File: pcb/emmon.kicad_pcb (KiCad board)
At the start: 2 copper layers, 114.3 x 97.8 mm, 37 parts, among them J1 PULSES_CONNECTOR, J2 Conn_01x06, J3 POWER_CONNECTOR, U1 DS3231MZ, U2 AT24CS32-SSHM, U3 ESP-12E, U4 Ai-Thinker-Ra-01, U5 AMS1117-3.3

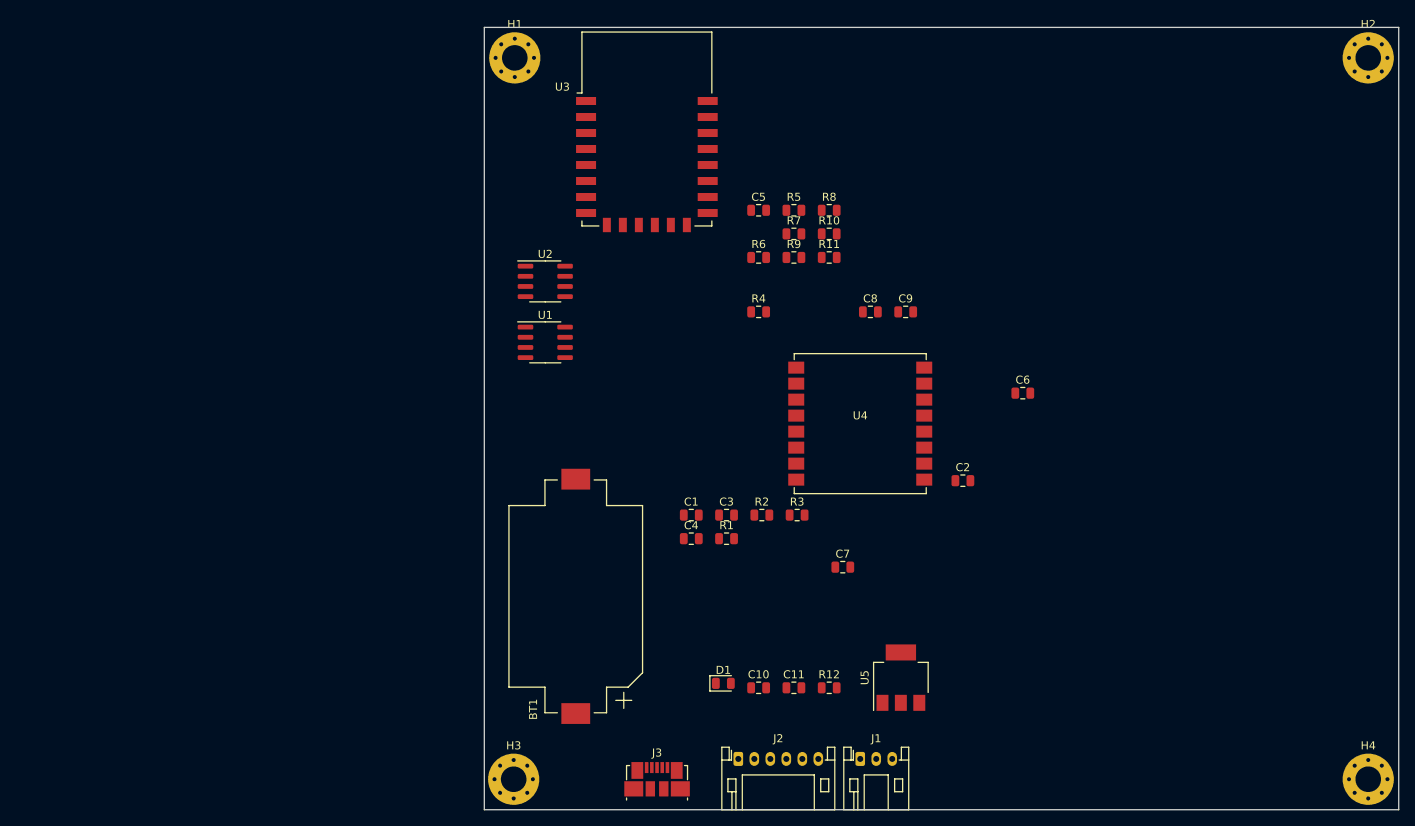
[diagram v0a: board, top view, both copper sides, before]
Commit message: se avanza en el ruteo de pistas
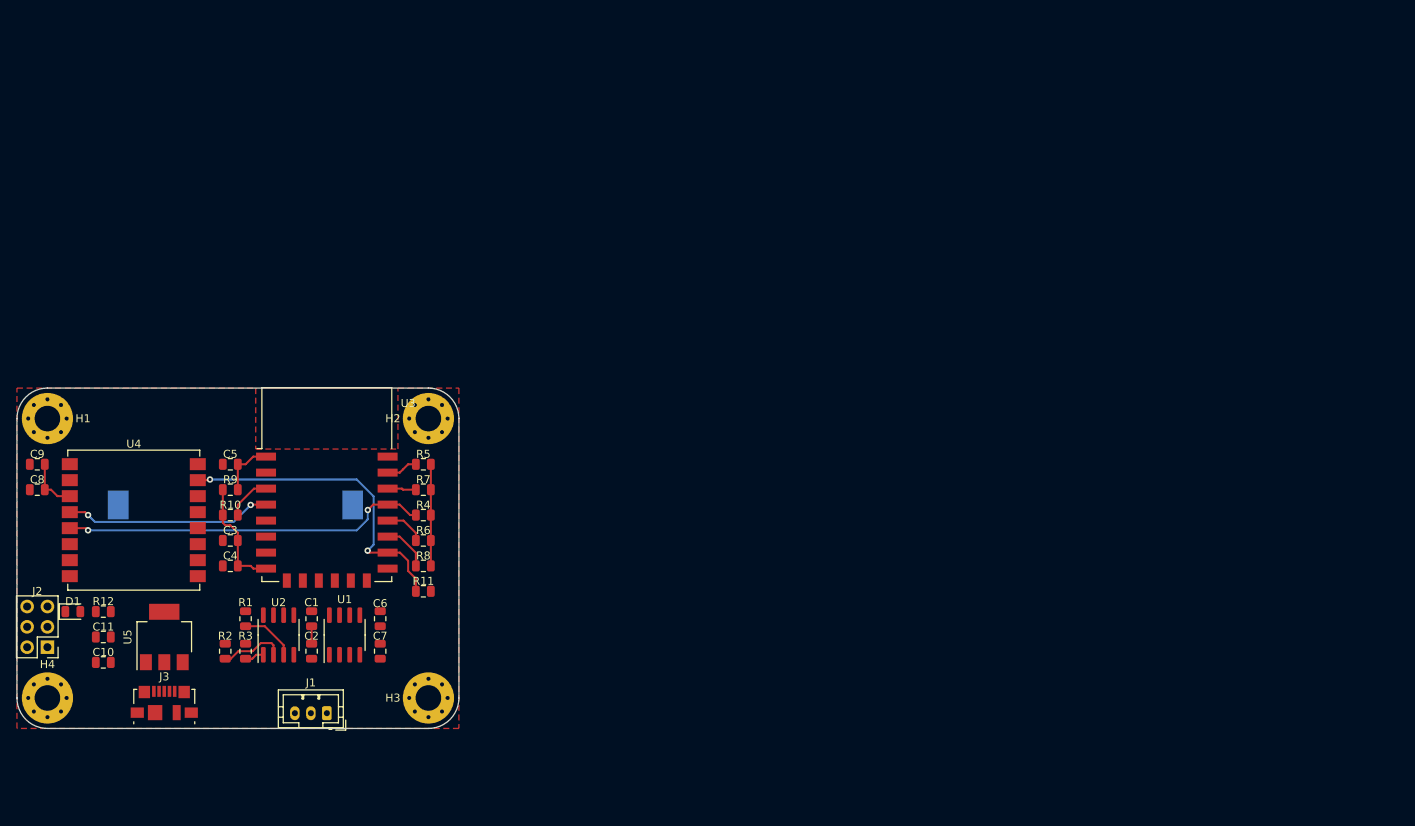
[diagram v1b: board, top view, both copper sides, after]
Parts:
- BT1: moved to B.Cu
- J1: footprint Connector_JST:JST_PH_S3B-PH-K_1x03_P2.00mm_Horizontal -> Connector_JST:JST_PH_B3B-PH-K_1x03_P2.00mm_Vertical
- J2: value Conn_01x06 -> PROG_CONNECTOR; footprint Connector_JST:JST_PH_S6B-PH-K_1x06_P2.00mm_Horizontal -> Connector_PinHeader_2.54mm:PinHeader_2x03_P2.54mm_Vertical
- moved H4 165.4 mm to (99.1, 118.1)
- moved H2 125.8 mm to (146.7, 83.2)
- moved C9 110.2 mm to (97.8, 88.9), turned to 180 degrees
- moved C8 106.5 mm to (97.8, 92.1), turned to 180 degrees
- moved U5 92.2 mm to (113.7, 110.5)
- moved U4 91.6 mm to (109.9, 95.9)
- moved R12 91.2 mm to (106.0, 107.3)
- moved J2 87.5 mm to (99.1, 111.8), turned to 180 degrees
- moved C11 86.6 mm to (106.0, 110.5), turned to 180 degrees
- moved C6 85.1 mm to (140.7, 108.2), turned to 270 degrees
- moved C2 84.2 mm to (132.1, 112.3), turned to 270 degrees
- moved R10 82.7 mm to (121.9, 95.2)
- moved C10 82.0 mm to (106.0, 113.7)
- moved D1 81.8 mm to (102.2, 107.3)
- moved R9 76.2 mm to (121.9, 92.1)
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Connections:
- J2 pad 2: TX -> (no net)
- J2 pad 3: ALARM -> GND
- J2 pad 4: PULSES -> (no net)
- J2 pad 5: RST -> (no net)
- J2 pad 6: GND -> (no net)
- J3 pad 6: Net-(J3-Pad6) -> GND
- U3 pad 22: TX -> (no net)
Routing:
- net DIO0: track 0.00 -> 45.9 mm, vias 0 -> 2
- net NSS: track 0.00 -> 39.8 mm, vias 0 -> 2
- net +3V3: track 0.00 -> 35.9 mm
- net RESET: track 0.00 -> 25.9 mm, vias 0 -> 2
- net Net-(R2-Pad2): track 0.00 -> 8.15 mm
- net RST: track 0.00 -> 7.10 mm
- net Net-(R1-Pad2): track 0.00 -> 6.95 mm
- net SDA: track 0.00 -> 6.00 mm
- net Net-(R10-Pad2): track 0.00 -> 5.65 mm
- net PULSES: track 0.00 -> 5.11 mm
- net ALARM: track 0.00 -> 3.96 mm
- net SCL: track 0.00 -> 3.58 mm
- net Net-(R3-Pad2): track 0.00 -> 2.43 mm
- added copper zone on F.Cu, net GND
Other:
- board size 114.3 x 97.8 mm -> 55.2 x 42.5 mm

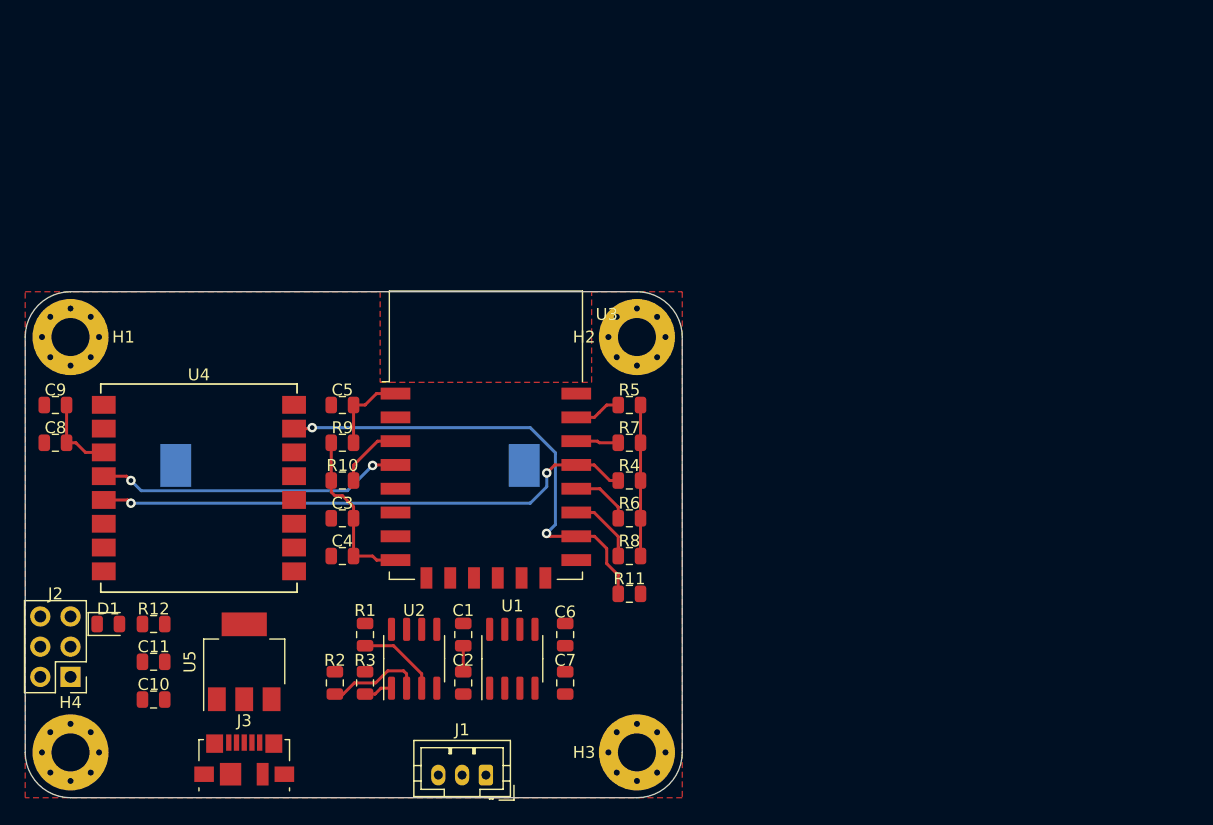
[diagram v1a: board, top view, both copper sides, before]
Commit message: se completa el esquemático y se avanza en el posicionamiento del pcb
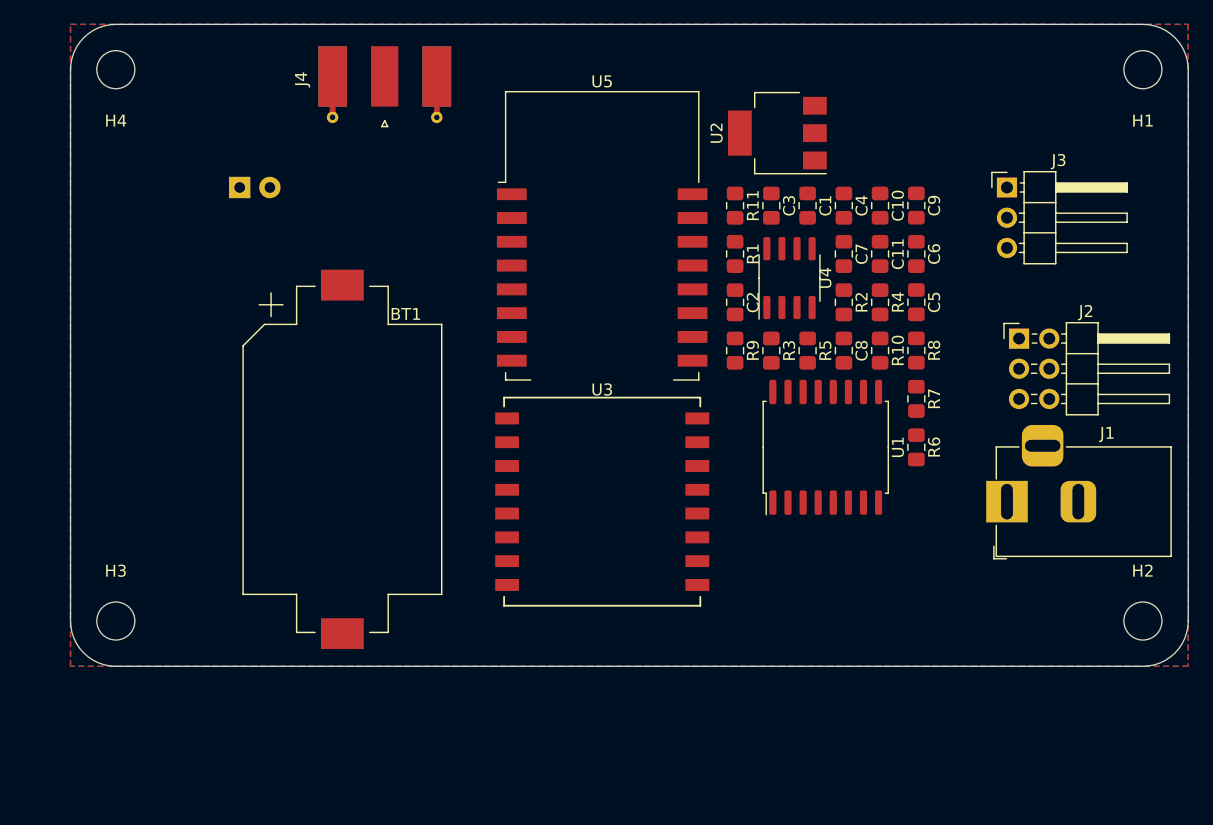
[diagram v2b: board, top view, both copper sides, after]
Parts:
- removed R12: 12K, Resistor_SMD:R_0805_2012Metric
- added J4: ANTENNA_CONNECTOR, Connector_Coaxial:SMA_Molex_73251-1153_EdgeMount_Horizontal, F.Cu at (125.5, 63.0)
- BT1: moved to F.Cu
- C1: footprint Capacitor_SMD:C_0805_2012Metric -> Capacitor_SMD:C_0805_2012Metric_Pad1.15x1.40mm_HandSolder
- C10: value 10u -> 1u; footprint Capacitor_SMD:C_0805_2012Metric -> Capacitor_SMD:C_0805_2012Metric_Pad1.15x1.40mm_HandSolder
- C11, C3, C6, C8: value 10u -> 100n; footprint Capacitor_SMD:C_0805_2012Metric -> Capacitor_SMD:C_0805_2012Metric_Pad1.15x1.40mm_HandSolder
- C2: value 100n -> 1u; footprint Capacitor_SMD:C_0805_2012Metric -> Capacitor_SMD:C_0805_2012Metric_Pad1.15x1.40mm_HandSolder
- C4: value 100n -> 10u; footprint Resistor_SMD:R_0805_2012Metric -> Capacitor_SMD:C_0805_2012Metric_Pad1.15x1.40mm_HandSolder
- C5: value 47p -> 10u; footprint Capacitor_SMD:C_0805_2012Metric -> Capacitor_SMD:C_0805_2012Metric_Pad1.15x1.40mm_HandSolder
- C7: value 100n -> 1u; footprint Resistor_SMD:R_0805_2012Metric -> Capacitor_SMD:C_0805_2012Metric_Pad1.15x1.40mm_HandSolder
- C9: value 100n -> 470p; footprint Resistor_SMD:R_0805_2012Metric -> Capacitor_SMD:C_0805_2012Metric_Pad1.15x1.40mm_HandSolder
- D1: footprint LED_SMD:LED_0805_2012Metric -> LED_THT:LED_D3.0mm; moved to B.Cu
- H1, H2, H3, H4: value MountingHole_Pad -> MountingHole; footprint MountingHole:MountingHole_3.2mm_M3_Pad_Via -> MountingHole:MountingHole_3.2mm_M3
- J1: value PULSES_CONNECTOR -> POWER_CONNECTOR; footprint Connector_JST:JST_PH_B3B-PH-K_1x03_P2.00mm_Vertical -> Connector_BarrelJack:BarrelJack_Horizontal
- J2: footprint Connector_PinHeader_2.54mm:PinHeader_2x03_P2.54mm_Vertical -> Connector_PinHeader_2.54mm:PinHeader_2x03_P2.54mm_Horizontal
- J3: value POWER_CONNECTOR -> SENSOR_CONNECTOR; footprint Connector_USB:USB_Micro-B_Molex_47346-0001 -> Connector_PinHeader_2.54mm:PinHeader_1x03_P2.54mm_Horizontal
- R1, R10, R11, R2, R3, R4, R5, R6, R7, R8, R9: footprint Resistor_SMD:R_0805_2012Metric -> Resistor_SMD:R_0805_2012Metric_Pad1.15x1.40mm_HandSolder
- U1: value DS3231MZ -> DS3231M; footprint Package_SO:SOIC-8_3.9x4.9mm_P1.27mm -> Package_SO:SOIC-16W_7.5x10.3mm_P1.27mm
- U2: value AT24CS32-SSHM -> AMS1117-3.3; footprint Package_SO:SOIC-8_3.9x4.9mm_P1.27mm -> Package_TO_SOT_SMD:SOT-223-3_TabPin2
- U3: value ESP-12E -> Ai-Thinker-Ra-01; footprint RF_Module:ESP-12E -> RF_Module:Ai-Thinker-Ra-01-LoRa
- U4: value Ai-Thinker-Ra-01 -> AT24CS32-SSHM; footprint RF_Module:Ai-Thinker-Ra-01-LoRa -> Package_SO:SOIC-8_3.9x4.9mm_P1.27mm
- U5: value AMS1117-3.3 -> ESP-12S; footprint Package_TO_SOT_SMD:SOT-223-3_TabPin2 -> ESP8266:ESP-12S
- moved H1 92.9 mm to (189.2, 60.7)
- moved J2 84.7 mm to (178.8, 83.3), turned to 0 degrees
- moved J3 80.2 mm to (177.8, 70.6)
- moved C9 74.3 mm to (170.2, 72.1), turned to 270 degrees
- moved C10 73.9 mm to (167.1, 72.1), turned to 90 degrees
- moved C11 70.1 mm to (167.1, 76.2), turned to 270 degrees
- moved C8 66.7 mm to (164.1, 84.3), turned to 90 degrees
- moved H4 57.5 mm to (102.9, 60.7)
- moved U2 53.7 mm to (158.5, 66.0), turned to 180 degrees
- moved R2 53.4 mm to (164.1, 80.3), turned to 90 degrees
- moved U4 52.7 mm to (159.5, 78.2), turned to 90 degrees
- moved C4 51.4 mm to (164.1, 72.1), turned to 270 degrees
- moved J1 49.5 mm to (177.8, 97.0)
- moved C5 49.0 mm to (170.2, 80.3), turned to 270 degrees
- moved H2 48.8 mm to (189.2, 107.1)
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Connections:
- C1 pad 1: +3V3 -> GND
- C1 pad 2: GND -> +5V
- C10 pad 1: GND -> +3V3
- C10 pad 2: +5V -> GND
- C5 pad 1: RST -> +3V3
- C9 pad 1: +3V3 -> RST
- H1 pad 1: GND -> (no net)
- H2 pad 1: GND -> (no net)
- H3 pad 1: GND -> (no net)
- H4 pad 1: GND -> (no net)
- J1 pad 1: +3V3 -> +5V
- J1 pad 2: PULSES -> GND
- J2 pad 1: +3V3 -> TX
- J2 pad 2: (no net) -> +3V3
- J2 pad 3: GND -> RST
- J2 pad 5: (no net) -> RX
- J2 pad 6: (no net) -> GND
- J3 pad 1: +5V -> +3V3
- J3 pad 2: (no net) -> PULSES
- J3 pad 3: (no net) -> GND
- R1 pad 1: +3V3 -> Net-(D1-Pad2)
- R1 pad 2: Net-(R1-Pad2) -> +3V3
- R10 pad 2: Net-(R10-Pad2) -> RST
- R4 pad 2: DIO0 -> Net-(R4-Pad2)
- R5 pad 1: +3V3 -> SDA
- R5 pad 2: ALARM -> +3V3
- R6 pad 1: +3V3 -> SCL
- R6 pad 2: PULSES -> +3V3
- R7 pad 1: +3V3 -> PULSES
- R7 pad 2: SCL -> +3V3
- R8 pad 1: +3V3 -> ALARM
- R8 pad 2: SDA -> +3V3
- R9 pad 1: +3V3 -> EN
- R9 pad 2: RST -> +3V3
- U1 pad 2: +3V3 -> +BATT
- U1 pad 6: +BATT -> GND
- U1 pad 7: SDA -> GND
- U1 pad 8: SCL -> GND
- U2 pad 1: Net-(R3-Pad2) -> GND
- U2 pad 2: Net-(R2-Pad2) -> +3V3
- U2 pad 3: Net-(R1-Pad2) -> +5V
- U3 pad 1: RST -> ANT
- U3 pad 12: (no net) -> SCK
- U3 pad 13: (no net) -> MISO
- U3 pad 14: (no net) -> MOSI
- U3 pad 15: GND -> NSS
- U3 pad 16: NSS -> GND
- U3 pad 2: (no net) -> GND
- U3 pad 3: Net-(R10-Pad2) -> +3V3
- U3 pad 5: SCK -> (no net)
- U3 pad 6: MISO -> (no net)
- U3 pad 7: MOSI -> (no net)
- U3 pad 8: +3V3 -> (no net)
- U3 pad 9: (no net) -> GND
- U4 pad 1: (no net) -> Net-(R4-Pad2)
- U4 pad 2: GND -> Net-(R3-Pad2)
- U4 pad 3: +3V3 -> Net-(R2-Pad2)
- U4 pad 4: RESET -> GND
- U4 pad 5: DIO0 -> SDA
- U4 pad 6: (no net) -> SCL
- U4 pad 7: (no net) -> GND
- U4 pad 8: (no net) -> +3V3
- U5 pad 1: GND -> RST
- U5 pad 2: +3V3 -> (no net)
- U5 pad 3: +5V -> EN
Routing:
- net DIO0: track 45.9 -> 0.00 mm, vias 2 -> 0
- net NSS: track 39.8 -> 0.00 mm, vias 2 -> 0
- net +3V3: track 35.9 -> 0.00 mm
- net RESET: track 25.9 -> 0.00 mm, vias 2 -> 0
- net Net-(R2-Pad2): track 8.15 -> 0.00 mm
- net RST: track 7.10 -> 0.00 mm
- net Net-(R1-Pad2): track 6.95 -> 0.00 mm
- net SDA: track 6.00 -> 0.00 mm
- net Net-(R10-Pad2): track 5.65 -> 0.00 mm
- net PULSES: track 5.11 -> 0.00 mm
- net ALARM: track 3.96 -> 0.00 mm
- net SCL: track 3.58 -> 0.00 mm
- net Net-(R3-Pad2): track 2.43 -> 0.00 mm
- added copper zone on B.Cu, net GND
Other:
- board size 55.2 x 42.5 mm -> 94 x 54 mm
- net class Default: clearance 0.2 -> 0.254; trace_width 0.25 -> 0.3048; via_dia 0.8 -> 2; via_drill 0.4 -> 1.5
- net class Power added: clearance 0.254, trace_width 0.6096, via_dia 2, via_drill 1.5
- rule trace_clearance: 0.2 -> 0.254

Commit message: se eliminan archivos temporales
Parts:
- D1: value LED_Small -> LED_POWER
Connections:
- J2 pad 4: (no net) -> SDA
